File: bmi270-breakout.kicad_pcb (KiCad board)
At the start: 2 copper layers, 16.5 x 20.3 mm, 16 parts, among them CN1 AFC10-S04QCA-00, CN2 AFC10-S04QCA-00, J1 Conn_01x06_Pin, J2 Conn_01x04_Pin, U1 BMI270

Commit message: redo layout
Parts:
- moved J2 2.54 mm to (157.5, 99.1)
- moved C1 1.27 mm to (153.4, 102.6)
- moved C2 1.27 mm to (153.4, 100.6)
- moved CN1 1.27 mm to (151.1, 95.9)
- moved H1 1.27 mm to (157.5, 95.0)
- moved H2 1.27 mm to (157.5, 110.5)
- moved J1 1.27 mm to (144.8, 96.5)
- moved JP1 1.27 mm to (151.1, 101.3)
- moved R1 1.27 mm to (148.8, 102.6)
- moved R2 1.27 mm to (148.8, 100.6)
- moved R3 1.27 mm to (148.5, 98.6)
- moved R4 1.27 mm to (148.6, 104.6)
- moved R5 1.27 mm to (150.7, 104.1)
- moved U1 1.27 mm to (151.1, 101.3)
- moved CN2 1.27 mm to (151.1, 109.9)
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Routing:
- net /INT1: track 7.95 -> 6.18 mm
- net /XCL: track 10.1 -> 8.54 mm
- net /XDA: track 12.0 -> 10.7 mm
- net GND: vias 15 -> 16

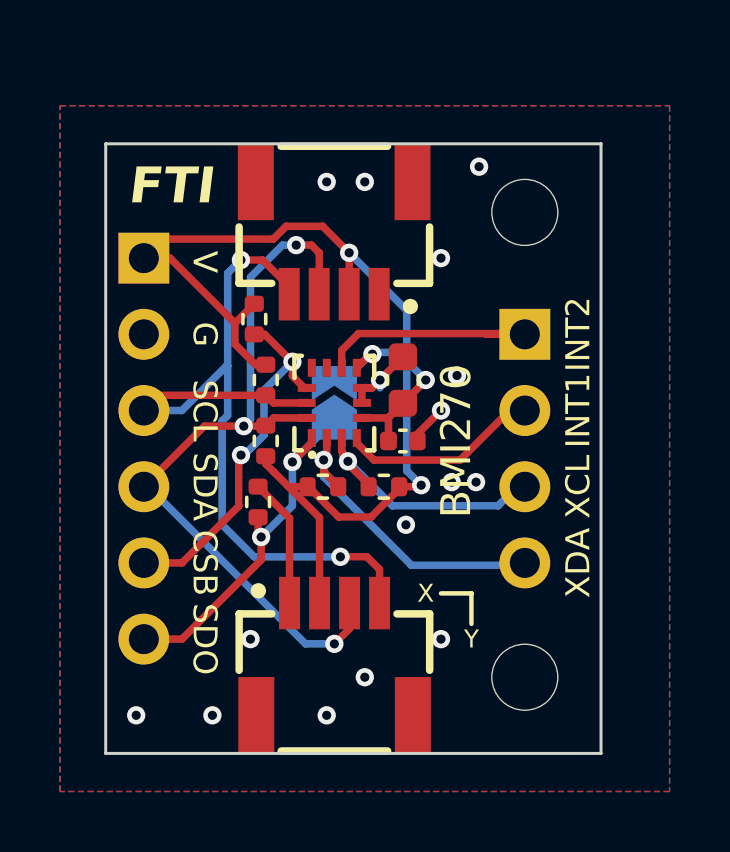
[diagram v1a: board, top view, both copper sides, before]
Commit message: use higher pullup, refine schematic
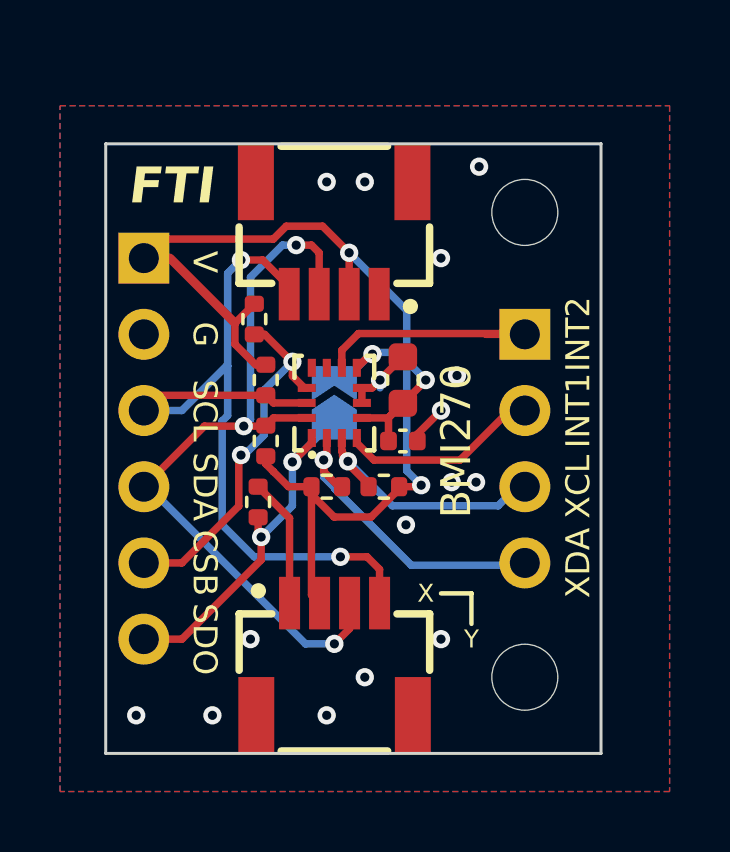
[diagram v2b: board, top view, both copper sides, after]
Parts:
- R1, R2, R3, R4, R5, R6: value 3.9k -> 4.7k
- moved R5 0.13 mm to (150.9, 104.1), turned to 180 degrees
- turned R6 to 0 degrees
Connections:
- C1 pad 1: +3.3V -> VCC
- C2 pad 1: +3.3V -> VCC
- CN1 pad 2: +3.3V -> VCC
- CN2 pad 2: +3.3V -> VCC
- J1 pad 1: +3.3V -> VCC
- JP1 pad 2: +3.3V -> VCC
- R1 pad 2: +3.3V -> VCC
- R2 pad 1: +3.3V -> VCC
- R3 pad 1: +3.3V -> VCC
- R5 pad 1: +3.3V -> /XDA
- R5 pad 2: /XDA -> VCC
- R6 pad 1: +3.3V -> /XCL
- R6 pad 2: /XCL -> VCC
- U1 pad 5: +3.3V -> VCC
- U1 pad 8: +3.3V -> VCC
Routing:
- net +3.3V: track 44.3 -> 0.00 mm, vias 4 -> 0
- net VCC: track 0.00 -> 44.0 mm, vias 0 -> 4

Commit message: silkscreen
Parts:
- R3, R4: value 4.7k -> 10k
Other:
- board text added: "1.71~3.6V I2C 0x69"
- board text added: "ADDR 0x68"
- board text removed: "ADDR"
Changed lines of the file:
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@@
 		(tags "resistor")
 		(property "Reference" "R6"
-			(at 0 -1.27 360)
+			(at 0 -1.27 0)
 			(layer "F.SilkS")
 			(hide yes)
@@
 		)
 		(property "Value" "4.7k"
-			(at 0 1.17 360)
+			(at 0 1.17 0)
 			(layer "F.Fab")
 			(effects
@@
 		)
 		(fp_text user "${REFERENCE}"
-			(at 0 0 360)
+			(at 0 0 0)
 			(layer "F.Fab")
 			(effects
@@
 			)
 		)
-		(property "Value" "4.7k"
+		(property "Value" "10k"
 			(at 0 1.17 90)
 			(layer "F.Fab")
@@
 		(tags "resistor")
 		(property "Reference" "R5"
-			(at 0 -1.17 360)
+			(at 0 -1.17 0)
 			(layer "F.SilkS")
 			(hide yes)
@@
 		)
 		(property "Value" "4.7k"
-			(at 0 1.17 360)
+			(at 0 1.17 0)
 			(layer "F.Fab")
 			(effects
@@
 		)
 		(fp_text user "${REFERENCE}"
-			(at 0 0 360)
+			(at 0 0 0)
 			(layer "F.Fab")
 			(effects
@@
 			)
 		)
-		(property "Value" "4.7k"
+		(property "Value" "10k"
 			(at 0 1.17 90)
 			(layer "F.Fab")
@@
 		)
 	)
-	(gr_text "ADDR"
+	(gr_text "ADDR\n0x68"
 		(at 151.13 103.378 90)
 		(layer "B.SilkS")
 		(effects
 			(font
-				(size 1 1)
-				(thickness 0.15)
+				(size 0.8 0.8)
+				(thickness 0.1)
 			)
 			(justify left mirror)
@@
 	)
 	(gr_text "BMI270"
-		(at 157.48 93.726 0)
+		(at 152.146 93.98 0)
 		(layer "B.SilkS")
 		(effects
@@
 				(thickness 0.15)
 			)
-			(justify left mirror)
+			(justify mirror)
 		)
 	)
@@
 		)
 	)
+	(gr_text "1.71~3.6V\nI2C 0x69"
+		(at 152.527 96.393 0)
+		(layer "B.SilkS")
+		(effects
+			(font
+				(size 0.8 0.8)
+				(thickness 0.1)
+			)
+			(justify mirror)
+		)
+	)
